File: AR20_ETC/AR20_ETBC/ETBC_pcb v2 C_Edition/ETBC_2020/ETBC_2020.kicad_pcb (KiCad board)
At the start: 2 copper layers, 48 x 82.4 mm, 38 parts, among them IC1 MC33931EK, J1 Conn_02x09_Top_Bottom, J2 Conn_02x05_Odd_Even, Q1 NDS356AP, U1 ACM_2020

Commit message: Work in progress
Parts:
- moved C5 0.42 mm to (89.0, 62.8)
- moved C12 0.42 mm to (87.0, 62.5)
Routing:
- net TPS1_Filtered: track 56.3 -> 54.9 mm
- net GND: track 50.6 -> 49.5 mm
- net PWR: vias 2 -> 165
- added copper zone on B.Cu, net PWR

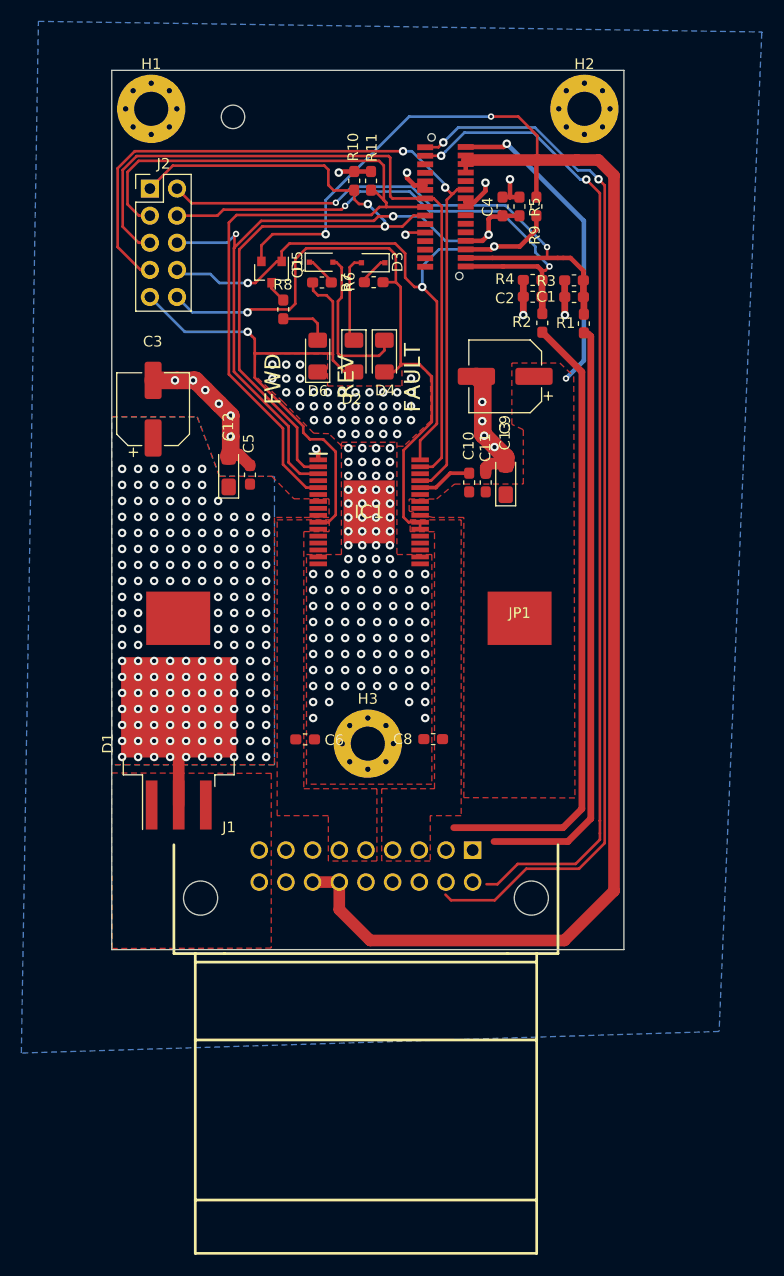
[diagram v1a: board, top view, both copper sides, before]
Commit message: V2.3  Better design Done
-New PCB 
-Got rid of superfluous Diode
-Got rid of poor choise Resistors in low pass filter
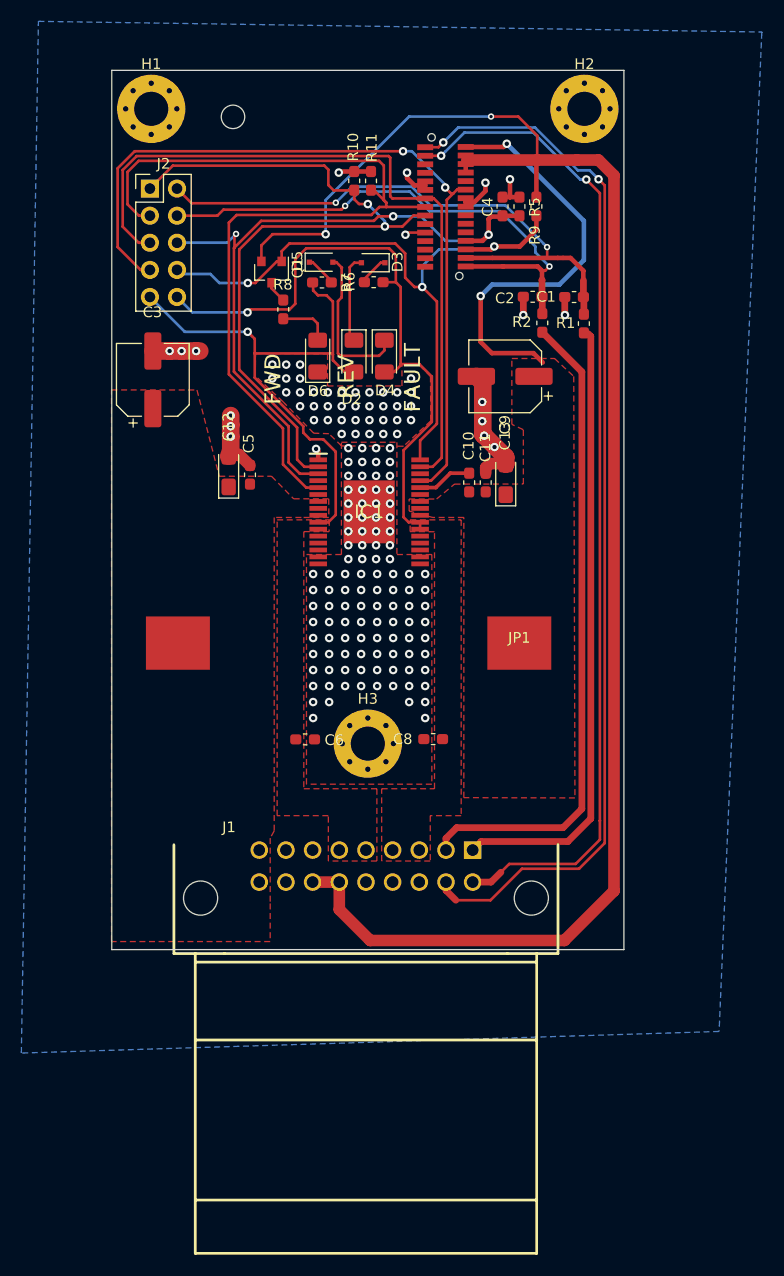
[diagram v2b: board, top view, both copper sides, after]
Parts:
- removed D1: WNS20S100CB, Package_TO_SOT_SMD:TO-263-3_TabPin2
- removed R3, R4: 4.7K, Resistor_SMD:R_0603_1608Metric_Pad1.05x0.95mm_HandSolder
- moved C3 2.75 mm to (79.8, 53.9)
- moved JP1 2.33 mm to (114.2, 78.6)
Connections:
- C10 pad 1: PWR -> 12V
- C11 pad 1: PWR -> 12V
- C12 pad 1: PWR -> 12V
- C13 pad 1: PWR -> 12V
- C3 pad 1: PWR -> 12V
- C5 pad 1: PWR -> 12V
- C9 pad 1: PWR -> 12V
- IC1 pad 25: PWR -> 12V
- IC1 pad 26: PWR -> 12V
- IC1 pad 7: PWR -> 12V
- IC1 pad 8: PWR -> 12V
- J1 pad 1: CANH -> TPS1
- J1 pad 10: (no net) -> CANH
- J1 pad 11: TPS2 -> CANL
- J1 pad 12: TPS1 -> GND
- J1 pad 2: CANL -> TPS2
- JP1 pad 1: PWR -> 12V
- JP1 pad 2: PWR -> 12V
- U1 pad 30: PWR -> 12V
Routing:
- net 12V: track 0.00 -> 39.9 mm, vias 0 -> 2
- net PWR: track 38.8 -> 0.00 mm, vias 165 -> 0
- net GND: track 49.5 -> 42.1 mm
- net TPS2: track 59.0 -> 61.5 mm
- net TPS1: track 55.5 -> 57.8 mm
- net CANH: track 92.6 -> 93.8 mm
- net CANL: track 99.2 -> 99.7 mm
- removed copper zone on B.Cu, net PWR
- removed copper zone on F.Cu, net PWR

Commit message: Updated Silk_scr and Generated Gerber
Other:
- board text added: "built upon Bachelor Thesis 2020 V1.1"
- board text removed: "Bachelor Thesis 2020 Electronic Throttle Body Controller V1.0"
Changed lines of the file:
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@@
   )
   (setup
-    (last_trace_width 1.651)
+    (last_trace_width 0.25)
     (user_trace_width 0.4318)
     (user_trace_width 0.635)
@@
       (psa4output false)
       (plotreference true)
-      (plotvalue true)
+      (plotvalue false)
       (plotinvisibletext false)
-      (padsonsilk false)
+      (padsonsilk true)
       (subtractmaskfromsilk false)
       (outputformat 1)
@@
     (add_net "Net-(D5-Pad1)")
     (add_net "Net-(D6-Pad2)")
-    (add_net "Net-(IC1-Pad12)")
-    (add_net "Net-(IC1-Pad13)")
-    (add_net "Net-(IC1-Pad14)")
-    (add_net "Net-(IC1-Pad19)")
-    (add_net "Net-(IC1-Pad20)")
-    (add_net "Net-(IC1-Pad21)")
-    (add_net "Net-(IC1-Pad24)")
-    (add_net "Net-(IC1-Pad27)")
-    (add_net "Net-(IC1-Pad30)")
-    (add_net "Net-(IC1-Pad4)")
-    (add_net "Net-(IC1-Pad6)")
-    (add_net "Net-(IC1-Pad9)")
-    (add_net "Net-(J1-Pad12)")
-    (add_net "Net-(J1-Pad17)")
     (add_net "Net-(Q1-Pad3)")
-    (add_net "Net-(U1-Pad1)")
-    (add_net "Net-(U1-Pad10)")
-    (add_net "Net-(U1-Pad11)")
-    (add_net "Net-(U1-Pad12)")
-    (add_net "Net-(U1-Pad14)")
-    (add_net "Net-(U1-Pad22)")
-    (add_net "Net-(U1-Pad23)")
-    (add_net "Net-(U1-Pad25)")
-    (add_net "Net-(U1-Pad3)")
-    (add_net "Net-(U1-Pad5)")
-    (add_net "Net-(U1-Pad7)")
     (add_net OUT1)
     (add_net OUT2)
@@
   (module "ETBC_2020:Jumper PWR 25 26" (layer F.Cu)
     (at 114.2 78.575 180)
-    (fp_text reference JP1 (at 0 0.5) (layer F.SilkS)
+    (fp_text reference JP1 (at 0.84 -4.985) (layer F.SilkS)
       (effects (font (size 1 1) (thickness 0.15)))
     )
@@
     )
   )
+  (gr_text "built upon\nBachelor Thesis \n2020\nV1.1" (at 117.85 68.3 270) (layer F.SilkS)
+    (effects (font (size 2 2) (thickness 0.15)) (justify left))
+  )
   (gr_poly (pts (xy 96.025 99.65) (xy 91.05 99.65) (xy 91.05 94) (xy 96.025 94)) (layer B.Mask) (width 0.1))
   (gr_poly (pts (xy 105.975 104.475) (xy 98.675 104.475) (xy 98.675 99.6) (xy 105.975 99.6)) (layer B.Mask) (width 0.1))
@@
   (gr_poly (pts (xy 93.06 65.1) (xy 96.32 65.1) (xy 96.32 66.13) (xy 94.28 66.1275) (xy 94.28 66.7525) (xy 91.2 66.75) (xy 91.2 67.17) (xy 76.2 67.16875) (xy 76.2 64.9) (xy 89.99 64.9) (xy 89.99 62.99) (xy 90.98 62.99)) (layer F.Mask) (width 0.1))
   (gr_line (start 124 24.892) (end 124 107.304974) (layer Edge.Cuts) (width 0.1))
-  (gr_text "Bachelor Thesis 2020\nElectronic Throttle Body Controller\nV1.0" (at 114.3889 93.6371 270) (layer B.SilkS)
-    (effects (font (size 2 2) (thickness 0.15)) (justify left mirror))
-  )
   (gr_line (start 76 107.304974) (end 76 24.892) (layer Edge.Cuts) (width 0.1))
   (gr_line (start 124 24.892) (end 76 24.892) (layer Edge.Cuts) (width 0.1))
@@
   (segment (start 115.704999 41.954999) (end 115.704999 41.404999) (width 0.25) (layer B.Cu) (net 3))
   (segment (start 103.925 36.25) (end 99.225 36.25) (width 0.25) (layer B.Cu) (net 3))
-  (segment (start 109.175 32.0746) (end 112.7254 32.0746) (width 0.4318) (layer F.Cu) (net 23))
-  (via (at 113.025 31.775) (size 0.8) (drill 0.4) (layers F.Cu B.Cu) (net 23))
-  (segment (start 112.7254 32.0746) (end 113.025 31.775) (width 0.4318) (layer F.Cu) (net 23))
-  (segment (start 120.25 42.675) (end 117.95 44.975) (width 0.4318) (layer B.Cu) (net 23))
-  (segment (start 113.025 31.775) (end 120.25 39) (width 0.4318) (layer B.Cu) (net 23))
-  (segment (start 120.25 39) (end 120.25 42.675) (width 0.4318) (layer B.Cu) (net 23))
-  (segment (start 117.95 44.975) (end 111.65 44.975) (width 0.4318) (layer B.Cu) (net 23))
-  (via (at 110.575 46.05) (size 0.8) (drill 0.4) (layers F.Cu B.Cu) (net 23))
-  (segment (start 111.65 44.975) (end 110.575 46.05) (width 0.4318) (layer B.Cu) (net 23))
-  (segment (start 111.625 51.4) (end 115.525 51.4) (width 0.4318) (layer F.Cu) (net 23))
-  (segment (start 115.525 51.4) (end 116.4 52.275) (width 0.4318) (layer F.Cu) (net 23))
-  (segment (start 110.575 46.05) (end 110.575 50.35) (width 0.4318) (layer F.Cu) (net 23))
-  (segment (start 110.575 50.35) (end 111.625 51.4) (width 0.4318) (layer F.Cu) (net 23))
   (via (at 111.325 40.3) (size 0.8) (drill 0.4) (layers F.Cu B.Cu) (net 4))
   (segment (start 111.325 40.3) (end 111.225 40.4) (width 0.25) (layer F.Cu) (net 4))
@@
   (segment (start 109.825 97.975) (end 110.625 97.175) (width 0.635) (layer F.Cu) (net 8))
   (segment (start 110.625 97.175) (end 118.75 97.175) (width 0.635) (layer F.Cu) (net 8))
+  (segment (start 107.325 97.975) (end 107.325 97.65) (width 0.25) (layer F.Cu) (net 9))
+  (segment (start 120.064989 53.152889) (end 116.3535 49.4414) (width 0.635) (layer F.Cu) (net 9))
+  (segment (start 107.325 96.875) (end 108.325 95.875) (width 0.635) (layer F.Cu) (net 9))
+  (segment (start 108.325 95.875) (end 118.3 95.875) (width 0.635) (layer F.Cu) (net 9))
+  (segment (start 107.325 97.975) (end 107.325 96.875) (width 0.635) (layer F.Cu) (net 9))
+  (segment (start 118.3 95.875) (end 120.064989 94.110011) (width 0.635) (layer F.Cu) (net 9))
+  (segment (start 120.064989 94.110011) (end 120.064989 53.152889) (width 0.635) (layer F.Cu) (net 9))
   (segment (start 99.675 44.75) (end 99.675 44.45) (width 0.25) (layer F.Cu) (net 10))
   (segment (start 99.675 44.45) (end 101.2 42.925) (width 0.25) (layer F.Cu) (net 10))
@@
   (segment (start 85.24 43.98) (end 82.5 43.98) (width 0.25) (layer B.Cu) (net 13))
   (segment (start 86.085 44.825) (end 85.24 43.98) (width 0.25) (layer B.Cu) (net 13))
-  (segment (start 107.325 97.975) (end 107.325 97.65) (width 0.25) (layer F.Cu) (net 9))
-  (segment (start 120.064989 53.152889) (end 116.3535 49.4414) (width 0.635) (layer F.Cu) (net 9))
-  (segment (start 107.325 96.875) (end 108.325 95.875) (width 0.635) (layer F.Cu) (net 9))
-  (segment (start 108.325 95.875) (end 118.3 95.875) (width 0.635) (layer F.Cu) (net 9))
-  (segment (start 107.325 97.975) (end 107.325 96.875) (width 0.635) (layer F.Cu) (net 9))
-  (segment (start 118.3 95.875) (end 120.064989 94.110011) (width 0.635) (layer F.Cu) (net 9))
-  (segment (start 120.064989 94.110011) (end 120.064989 53.152889) (width 0.635) (layer F.Cu) (net 9))
   (via (at 107.075 31.65) (size 0.8) (drill 0.4) (layers F.Cu B.Cu) (net 14))
   (segment (start 105.375 32.1) (end 106.625 32.1) (width 0.25) (layer F.Cu) (net 14))
@@
   (segment (start 95.3 50.1875) (end 95.3 48.625) (width 0.25) (layer F.Cu) (net 22))
   (segment (start 95.3 48.625) (end 94.85 48.175) (width 0.25) (layer F.Cu) (net 22))
+  (segment (start 109.175 32.0746) (end 112.7254 32.0746) (width 0.4318) (layer F.Cu) (net 23))
+  (via (at 113.025 31.775) (size 0.8) (drill 0.4) (layers F.Cu B.Cu) (net 23))
+  (segment (start 112.7254 32.0746) (end 113.025 31.775) (width 0.4318) (layer F.Cu) (net 23))
+  (segment (start 120.25 42.675) (end 117.95 44.975) (width 0.4318) (layer B.Cu) (net 23))
+  (segment (start 113.025 31.775) (end 120.25 39) (width 0.4318) (layer B.Cu) (net 23))
+  (segment (start 120.25 39) (end 120.25 42.675) (width 0.4318) (layer B.Cu) (net 23))
+  (segment (start 117.95 44.975) (end 111.65 44.975) (width 0.4318) (layer B.Cu) (net 23))
+  (via (at 110.575 46.05) (size 0.8) (drill 0.4) (layers F.Cu B.Cu) (net 23))
+  (segment (start 111.65 44.975) (end 110.575 46.05) (width 0.4318) (layer B.Cu) (net 23))
+  (segment (start 111.625 51.4) (end 115.525 51.4) (width 0.4318) (layer F.Cu) (net 23))
+  (segment (start 115.525 51.4) (end 116.4 52.275) (width 0.4318) (layer F.Cu) (net 23))
+  (segment (start 110.575 46.05) (end 110.575 50.35) (width 0.4318) (layer F.Cu) (net 23))
+  (segment (start 110.575 50.35) (end 111.625 51.4) (width 0.4318) (layer F.Cu) (net 23))
   (segment (start 90.975 45.325) (end 90.975 44.8) (width 0.25) (layer F.Cu) (net 24))
   (segment (start 92.075 46.425) (end 90.975 45.325) (width 0.25) (layer F.Cu) (net 24))
